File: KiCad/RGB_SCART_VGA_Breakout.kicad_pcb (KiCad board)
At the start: 2 copper layers, 81 x 40.5 mm, 23 parts, among them J1 SCART-F, J11 SJ1-3535NG, J3 DE15_Plug_HighDensity_Mountin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, J4 Conn_01x09, J5 Mounting, J6 Mounting, J7 Mounting, J8 Mounting

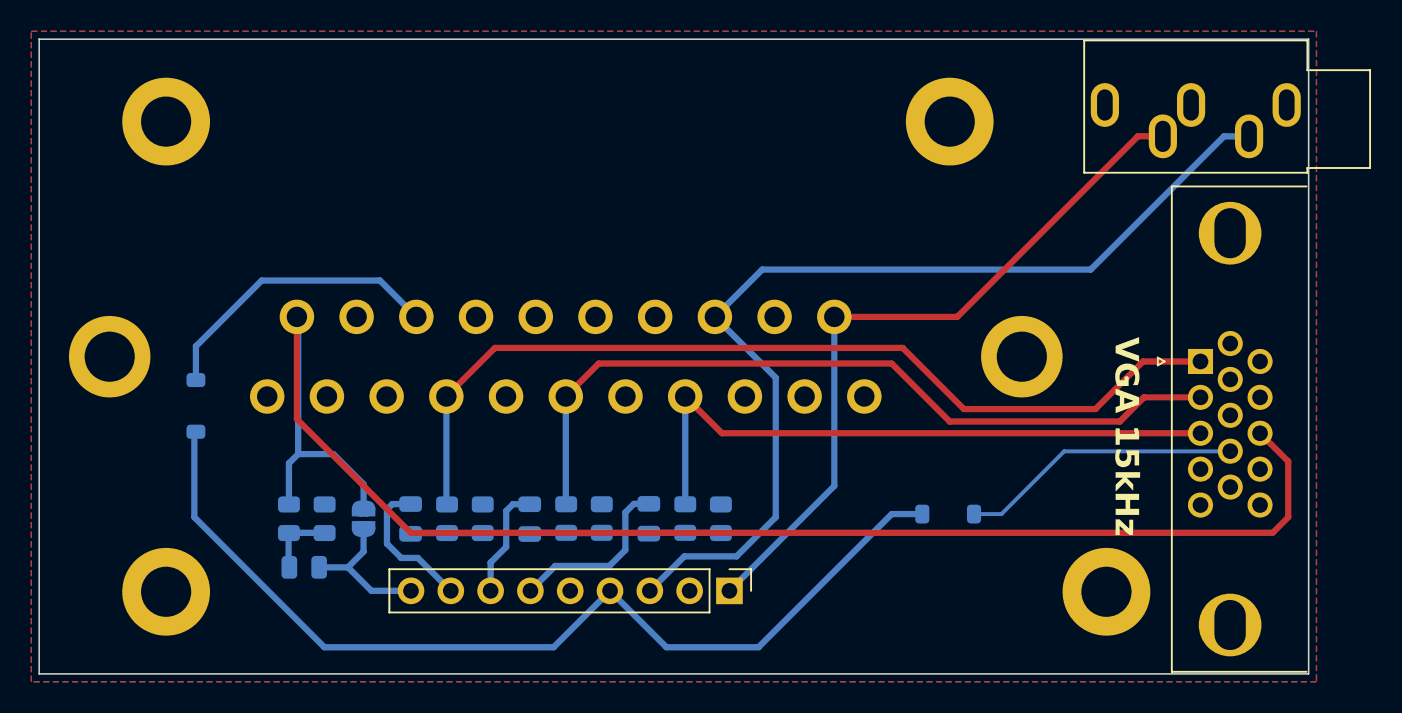
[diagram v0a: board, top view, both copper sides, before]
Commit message: Added blanking voltage divider / pulldown resistors with description. Expanded RGB load / voltage divider resistors description. VGA pins 7,8,10 connected to GND.
PCB version 1.1.
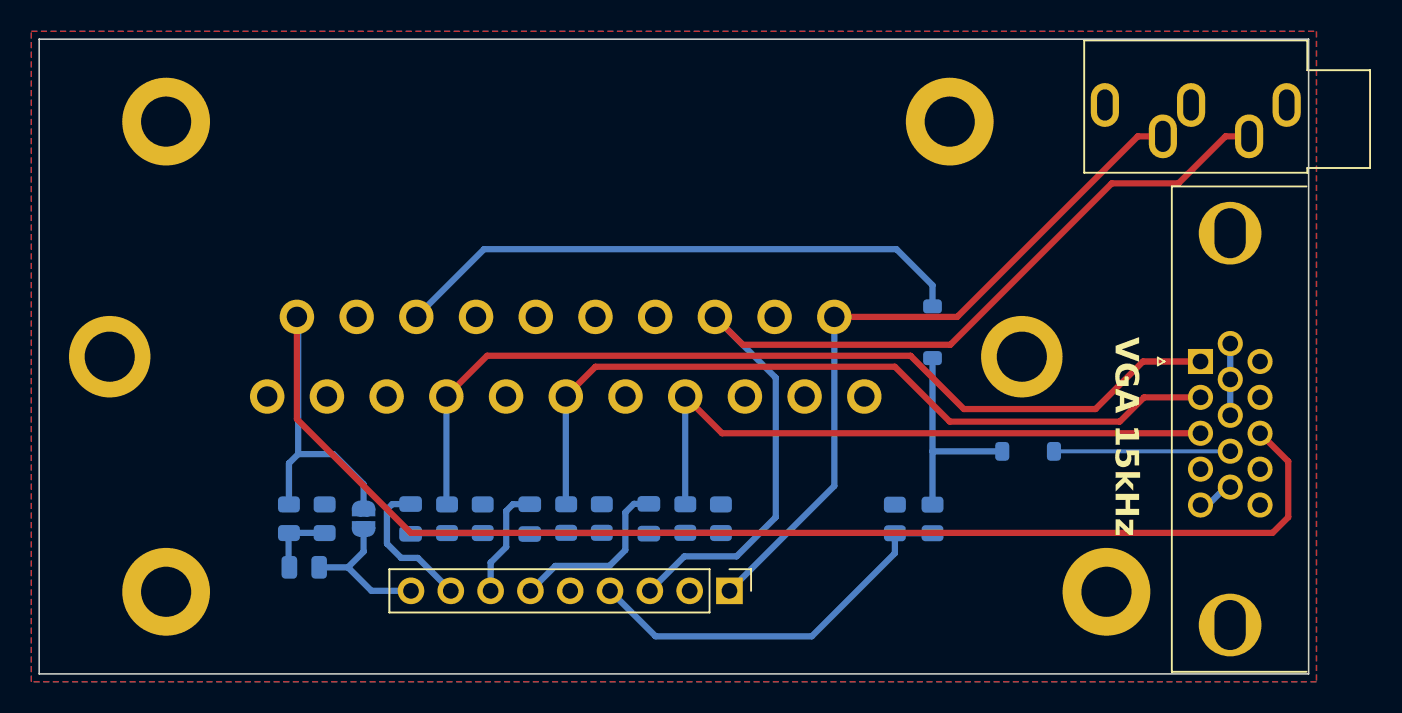
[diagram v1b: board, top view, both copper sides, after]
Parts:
- added R10: 2K3, Resistor_SMD:R_0805_2012Metric, B.Cu at (169.8, 94.4)
- added R9: 1K, Resistor_SMD:R_0805_2012Metric, B.Cu at (172.2, 94.4)
- moved D2 47.2 mm to (172.2, 82.5)
- moved D1 6.48 mm to (178.3, 90.1)
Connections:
- J4 pad 4: /BLANKING -> /BLANKING_DIV
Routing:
- net /BLANKING: track 62.0 -> 13.8 mm
- net /BLANKING_DIV: track 0.00 -> 25.4 mm
- net Net-(D2-A): track 18.9 -> 37.0 mm
- net GND: track 0.76 -> 7.71 mm
- net /VGA_5V: track 18.0 -> 11.3 mm
- net /AUDIO_L: track 63.2 -> 64.7 mm
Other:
- board text added: "V.1.1"
